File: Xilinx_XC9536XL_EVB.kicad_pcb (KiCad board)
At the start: 2 copper layers, 100 x 66 mm, 58 parts, among them IC1 ATTINY2313-P, P1 CONN_7X2, P2 CONN_2, P3 CONN_3X2, P4 CONN_5, P5 CONN_5, P6 CONN_12, P7 CONN_6, P8 CONN_8, SW1 SW_PUSH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

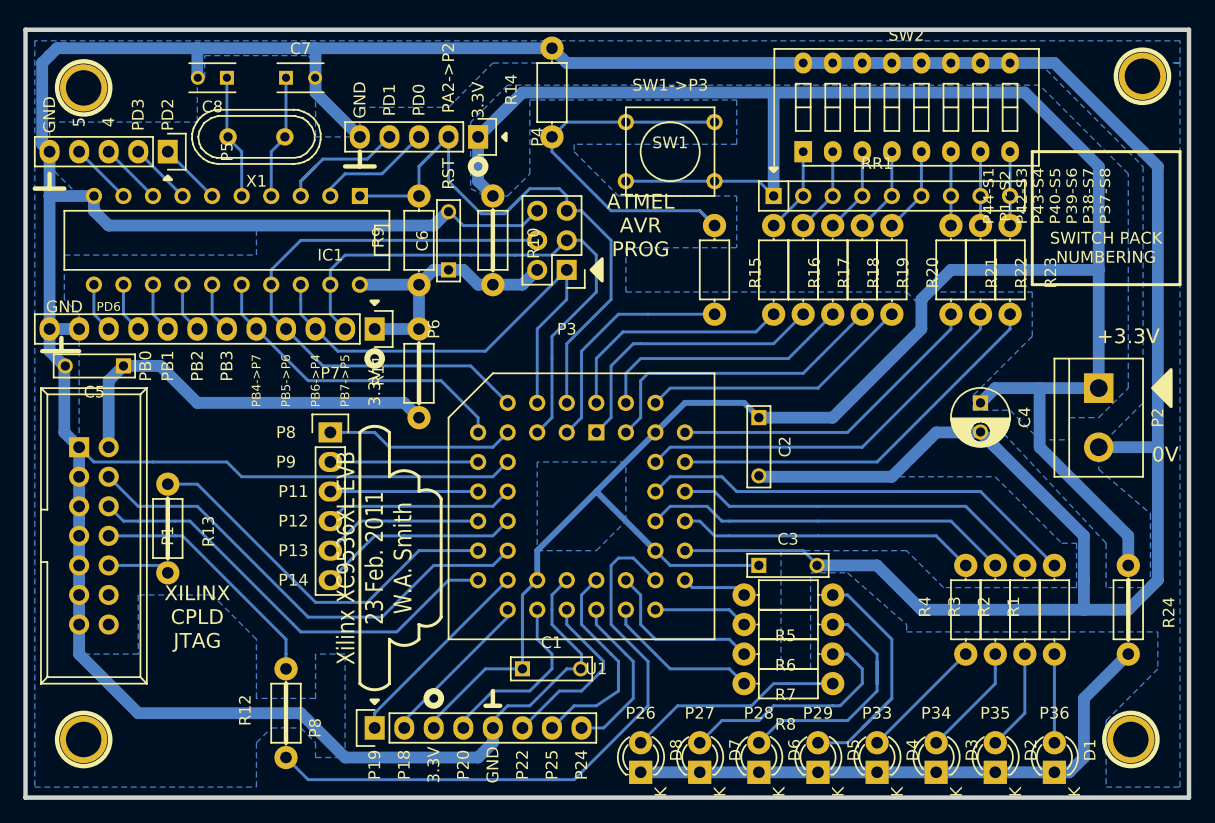
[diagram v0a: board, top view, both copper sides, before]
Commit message: switched to official footprint git repos since PRs have been accepted.
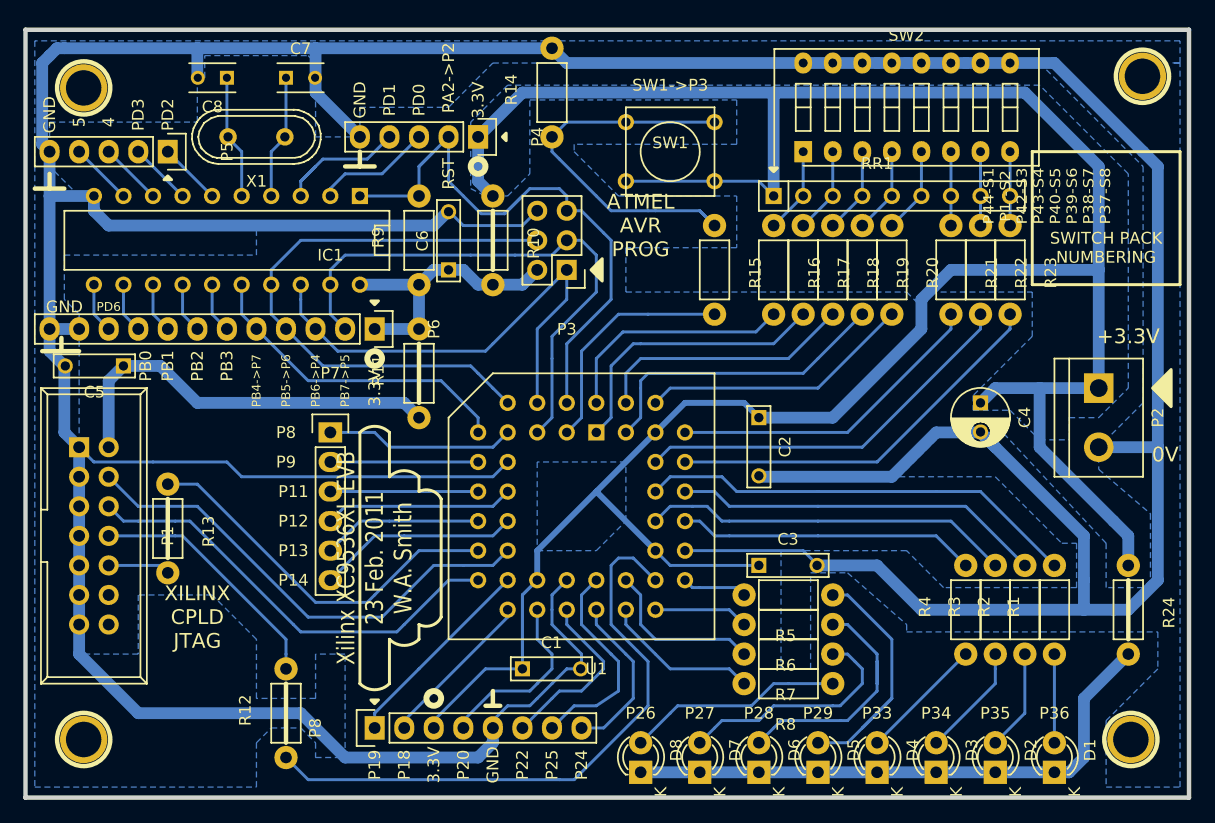
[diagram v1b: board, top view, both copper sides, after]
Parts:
- P1: footprint Connect_custom:IDC_Header_Straight_14pins -> Connect:IDC_Header_Straight_14pins
- R1, R10, R11, R12, R13, R14, R15, R16, R17, R18, R19, R2, R20, R21, R22, R23, R24, R3, R4, R5, R6, R7, R8, R9: footprint Resistors_ThroughHole_custom:Resistor_Horizontal_RM7mm -> Resistors_ThroughHole:Resistor_Horizontal_RM7mm
